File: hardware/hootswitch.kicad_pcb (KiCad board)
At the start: 2 copper layers, 100 x 88 mm, 127 parts, among them J1 Mini-DIN-4-G, J10 POWSEL, J11 TWI, J12 TWI, J2 Mini-DIN-4-G, J3 Mini-DIN-4-G, J4 Mini-DIN-4-G, J5 Mini-DIN-4-G, J6 Mini-DIN-4-G, J7 Barrel_Jack_MountingPin, J8 EXT_POW, J9 SW1, Q1 MMBT3904, Q10 MMBT3904, Q11 MMBT3904, Q12 MMBT3904, Q13 MMBT3904, Q14 MMBT3904, Q15 MMBT3904, Q16 MMBT3904, Q2 MMBT3904, Q3 MMBT3904, Q4 MMBT3904, Q5 MMBT3904, Q6 MMBT3904, Q7 MMBT3904, Q8 MMBT3904, Q9 MMBT3904, SW1 Switch1, U1 Pico, U10 LTV-357T, U11 LTV-357T, U2 LM1117-5.0, U3 ADuM1201AR, U4 ADuM1201AR, U5 ADuM1201AR, U6 ADuM1201AR, U7 ADuM1201AR, U8 LTV-357T, U9 LTV-357T

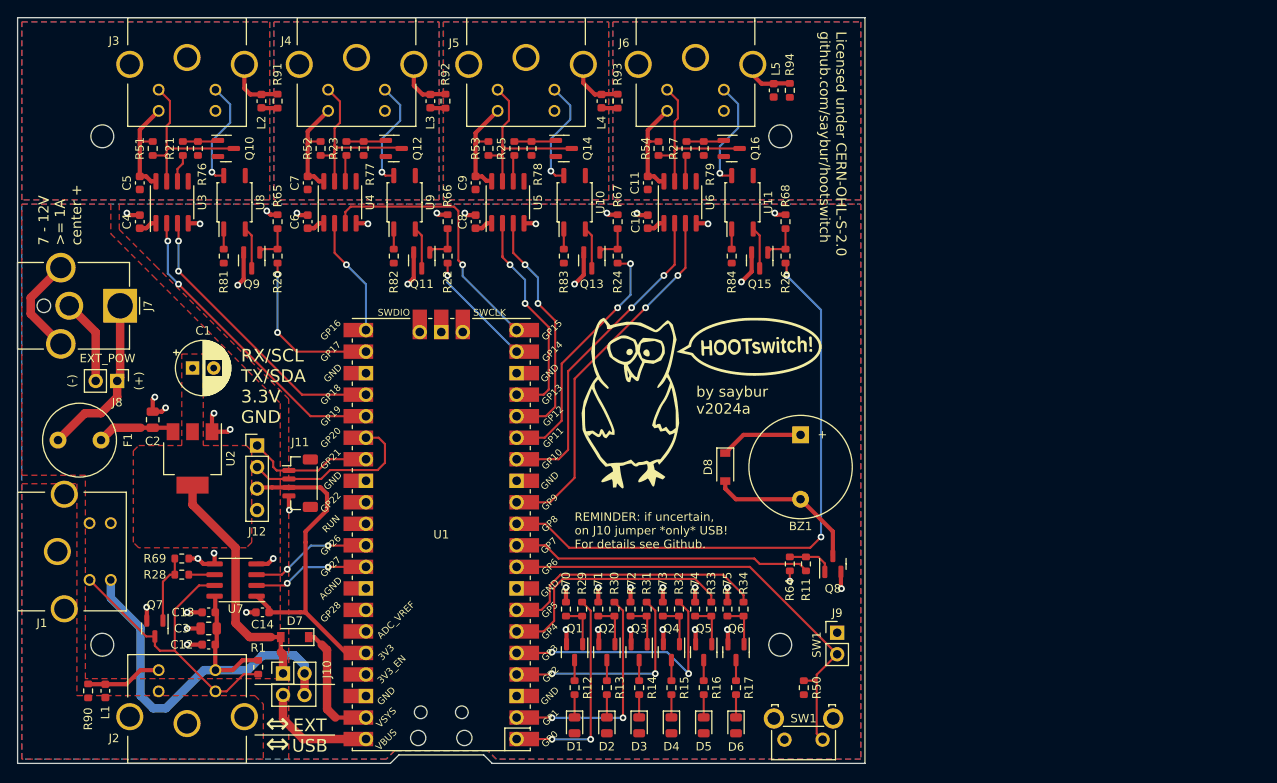
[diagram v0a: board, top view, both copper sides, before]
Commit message: Hardware Fork: Use Mosfets For Isolation
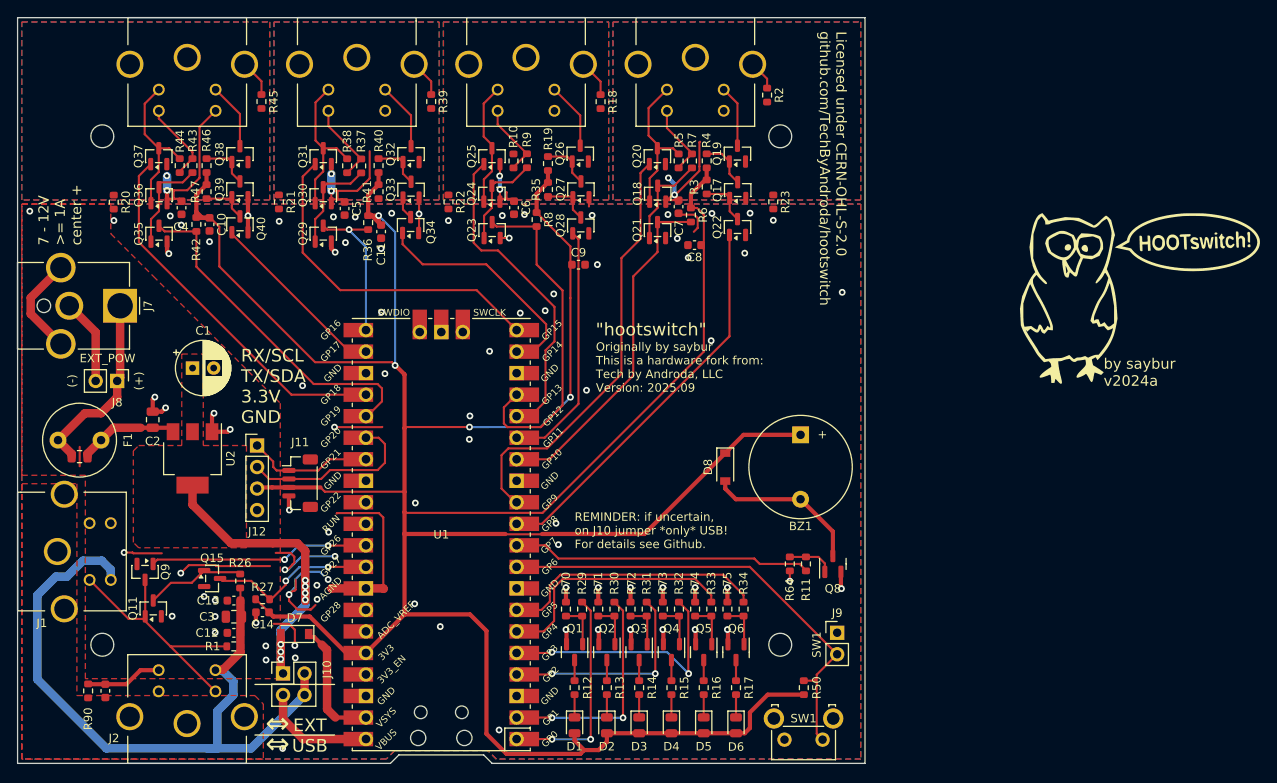
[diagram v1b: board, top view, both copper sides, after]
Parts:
- removed J3, J4, J5, J6: Mini-DIN-4-G, hootswitch:5749181-1
- removed L2, L3, L4, L5: DNP, Inductor_SMD:L_0603_1608Metric
- removed Q10, Q12, Q13, Q14, Q16, Q7: MMBT3904, Package_TO_SOT_SMD:SOT-23
- removed R24, R25, R28: 2K2, Resistor_SMD:R_0603_1608Metric
- removed R51, R52, R53, R54: 4K7, Resistor_SMD:R_0603_1608Metric
- removed R65, R66, R67, R68, R69, R76, R77, R78, R79: 10K, Resistor_SMD:R_0603_1608Metric
- removed R81, R82, R83, R84: 330, Resistor_SMD:R_0603_1608Metric
- removed R91, R92, R93, R94: 0, Resistor_SMD:R_0603_1608Metric
- removed U10, U11, U8, U9: LTV-357T, Package_SO:SO-4_4.4x3.9mm_P2.54mm
- removed U3, U4, U5, U6, U7: ADuM1201AR, Package_SO:SOIC-8_3.9x4.9mm_P1.27mm
- added F2: 500mA, Fuse:Fuse_0805_2012Metric, F.Cu at (67.3, 111.8)
- added J13: Mini-DIN-4-G, hootswitch:5749181-1, F.Cu at (140.0, 60.0)
- added J14: Mini-DIN-4-G, hootswitch:5749181-1, F.Cu at (120.0, 60.0)
- added J15: Mini-DIN-4-G, hootswitch:5749181-1, F.Cu at (100.0, 60.0)
- added J16: Mini-DIN-4-G, hootswitch:5749181-1, F.Cu at (80.0, 60.0)
- added Q17: 2N7002, Package_TO_SOT_SMD:SOT-23, F.Cu at (145.0, 80.3)
- added Q18: 2N7002, Package_TO_SOT_SMD:SOT-23, F.Cu at (135.5, 80.8)
- added Q19: 2N7002, Package_TO_SOT_SMD:SOT-23, F.Cu at (144.9, 76.0)
- added Q20: 2N7002, Package_TO_SOT_SMD:SOT-23, F.Cu at (135.5, 76.3)
- added Q21: 2N7002, Package_TO_SOT_SMD:SOT-23, F.Cu at (135.5, 85.1)
- added Q22: 2N7002, Package_TO_SOT_SMD:SOT-23, F.Cu at (145.0, 84.7)
- added Q23: 2N7002, Package_TO_SOT_SMD:SOT-23, F.Cu at (116.0, 85.1)
- added Q24: 2N7002, Package_TO_SOT_SMD:SOT-23, F.Cu at (116.0, 80.8)
- added Q25: 2N7002, Package_TO_SOT_SMD:SOT-23, F.Cu at (116.0, 76.3)
- added Q26: 2N7002, Package_TO_SOT_SMD:SOT-23, F.Cu at (126.4, 76.0)
- added Q27: 2N7002, Package_TO_SOT_SMD:SOT-23, F.Cu at (126.5, 80.3)
- added Q28: 2N7002, Package_TO_SOT_SMD:SOT-23, F.Cu at (126.5, 84.5)
- added Q29: 2N7002, Package_TO_SOT_SMD:SOT-23, F.Cu at (96.1, 85.5)
- added Q30: 2N7002, Package_TO_SOT_SMD:SOT-23, F.Cu at (96.1, 81.0)
- added Q31: 2N7002, Package_TO_SOT_SMD:SOT-23, F.Cu at (96.1, 76.3)
- added Q32: 2N7002, Package_TO_SOT_SMD:SOT-23, F.Cu at (106.4, 76.1)
- added Q33: 2N7002, Package_TO_SOT_SMD:SOT-23, F.Cu at (106.4, 80.3)
- added Q34: 2N7002, Package_TO_SOT_SMD:SOT-23, F.Cu at (106.4, 84.5)
- added Q35: 2N7002, Package_TO_SOT_SMD:SOT-23, F.Cu at (76.7, 85.5)
- added Q36: 2N7002, Package_TO_SOT_SMD:SOT-23, F.Cu at (76.7, 81.0)
- added Q37: 2N7002, Package_TO_SOT_SMD:SOT-23, F.Cu at (76.7, 76.3)
- added Q38: 2N7002, Package_TO_SOT_SMD:SOT-23, F.Cu at (86.2, 76.1)
- added Q39: 2N7002, Package_TO_SOT_SMD:SOT-23, F.Cu at (86.2, 80.3)
- added Q40: 2N7002, Package_TO_SOT_SMD:SOT-23, F.Cu at (86.2, 84.4)
- added R10: 4.7k, Resistor_SMD:R_0603_1608Metric, F.Cu at (118.5, 76.9)
- added R18: 33, Resistor_SMD:R_0603_1608Metric, F.Cu at (128.8, 69.9)
- added R19: 10k, Resistor_SMD:R_0603_1608Metric, F.Cu at (122.6, 77.2)
- added R2: 33, Resistor_SMD:R_0603_1608Metric, F.Cu at (148.4, 69.1)
- added R3: 10k, Resistor_SMD:R_0603_1608Metric, F.Cu at (141.3, 80.0)
- added R35: 10k, Resistor_SMD:R_0603_1608Metric, F.Cu at (122.6, 80.3)
- added R36: 1k, Resistor_SMD:R_0603_1608Metric, F.Cu at (101.4, 84.2)
- added R37: 4.7k, Resistor_SMD:R_0603_1608Metric, F.Cu at (100.5, 77.5)
- added R38: 4.7k, Resistor_SMD:R_0603_1608Metric, F.Cu at (98.9, 77.5)
- added R39: 33, Resistor_SMD:R_0603_1608Metric, F.Cu at (108.8, 69.9)
- added R4: 10k, Resistor_SMD:R_0603_1608Metric, F.Cu at (141.3, 76.9)
- added R40: 10k, Resistor_SMD:R_0603_1608Metric, F.Cu at (102.6, 77.5)
- added R41: 10k, Resistor_SMD:R_0603_1608Metric, F.Cu at (102.6, 80.5)
- added R42: 1k, Resistor_SMD:R_0603_1608Metric, F.Cu at (81.1, 84.4)
- added R43: 4.7k, Resistor_SMD:R_0603_1608Metric, F.Cu at (80.6, 77.5)
- added R44: 4.7k, Resistor_SMD:R_0603_1608Metric, F.Cu at (79.1, 77.5)
- added R45: 33, Resistor_SMD:R_0603_1608Metric, F.Cu at (88.8, 69.9)
- added R46: 10k, Resistor_SMD:R_0603_1608Metric, F.Cu at (82.3, 77.5)
- added R47: 10k, Resistor_SMD:R_0603_1608Metric, F.Cu at (82.3, 80.5)
- added R5: 4.7k, Resistor_SMD:R_0603_1608Metric, F.Cu at (138.0, 76.9)
- added R6: 1k, Resistor_SMD:R_0603_1608Metric, F.Cu at (139.5, 83.3)
- added R7: 4.7k, Resistor_SMD:R_0603_1608Metric, F.Cu at (139.6, 76.9)
- added R8: 1k, Resistor_SMD:R_0603_1608Metric, F.Cu at (121.2, 83.8)
- added R9: 4.7k, Resistor_SMD:R_0603_1608Metric, F.Cu at (120.1, 76.9)
- C10, C11, C8, C9: value 100nF -> 100N
- C4, C5, C6, C7: value 100nF -> 10n
- D7: value B5819W -> type="D" model="B5819W" lib=""
- Q11, Q15, Q9: value MMBT3904 -> 2N7002
- R20, R21, R22, R23, R26: value 2K2 -> 10k
- R27: value 2K2 -> 1k
- R90: value 0 -> 33
- moved R26 74.9 mm to (86.3, 126.5)
- moved Q15 74.7 mm to (83.0, 126.2), turned to 0 degrees
- moved R27 73.0 mm to (88.9, 128.6), turned to 0 degrees
- moved G*** 53.2 mm to (192.1, 93.1)
- moved Q11 51.9 mm to (76.0, 129.7), turned to 90 degrees
- moved C10 51.7 mm to (82.7, 84.4), turned to -90 degrees
- moved R23 50.8 mm to (149.2, 81.7), turned to -90 degrees
- moved C7 43.9 mm to (138.0, 82.3)
- moved Q9 38.9 mm to (75.0, 125.4)
- moved C11 32.0 mm to (102.9, 85.2)
- moved C8 26.0 mm to (139.9, 86.8), turned to 180 degrees
- moved C6 24.4 mm to (118.6, 82.4), turned to -90 degrees
- moved C5 24.4 mm to (98.6, 82.5)
- moved R20 20.4 mm to (71.3, 81.8), turned to -90 degrees
- moved C9 15.5 mm to (126.2, 89.2), turned to 0 degrees
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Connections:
- C11 pad 1: Net-(C11-Pad1) -> +3.3V
- C11 pad 2: Net-(C11-Pad2) -> GND
- C4 pad 1: +3.3V -> ADB1_GND
- C5 pad 1: Net-(C5-Pad1) -> ADB2_GND
- C5 pad 2: Net-(C5-Pad2) -> GND
- C6 pad 1: +3.3V -> ADB3_GND
- C7 pad 1: Net-(C7-Pad1) -> ADB4_GND
- C7 pad 2: Net-(C7-Pad2) -> GND
- C9 pad 1: Net-(C9-Pad1) -> +3.3V
- C9 pad 2: Net-(C9-Pad2) -> GND
- J1 pad 1: Net-(J2-Pad1) -> ADB_HOST_DAT
- J2 pad 1: Net-(J2-Pad1) -> ADB_HOST_DAT
- Q11 pad 1: Net-(Q11-Pad1) -> ADB_HOST_DAT
- Q11 pad 3: Net-(Q11-Pad3) -> Net-(Q11-D)
- Q15 pad 1: Net-(Q15-Pad1) -> Net-(Q11-D)
- Q15 pad 3: Net-(Q15-Pad3) -> /A_DI
- Q9 pad 1: Net-(Q9-Pad1) -> /A_DO
- Q9 pad 3: Net-(Q9-Pad3) -> ADB_HOST_DAT
- R1 pad 2: Net-(J2-Pad1) -> ADB_HOST_DAT
- R20 pad 1: /C1_PSW -> ADB1_GND
- R20 pad 2: Net-(Q9-Pad1) -> GND
- R21 pad 1: Net-(R21-Pad1) -> ADB2_GND
- R21 pad 2: Net-(Q10-Pad1) -> GND
- R22 pad 1: /C2_PSW -> ADB3_GND
- R22 pad 2: Net-(Q11-Pad1) -> GND
- R23 pad 1: Net-(R23-Pad1) -> ADB4_GND
- R23 pad 2: Net-(Q12-Pad1) -> GND
- R26 pad 1: /C4_PSW -> +5V
- R26 pad 2: Net-(Q15-Pad1) -> Net-(Q11-D)
- R27 pad 1: Net-(R27-Pad1) -> +3.3V
- R27 pad 2: Net-(Q16-Pad1) -> /A_DI
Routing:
- net +3.3V: track 58.0 -> 377.8 mm, vias 0 -> 4
- net GND: track 90.8 -> 138.2 mm, vias 43 -> 86
- net Net-(J2-Pad1): track 37.5 -> 0.00 mm
- net ADB_HOST_DAT: track 0.00 -> 31.3 mm
- net +5V: track 56.1 -> 86.0 mm
- net /C4_PSW: track 71.7 -> 46.2 mm, vias 2 -> 0
- net Net-(J4-Pad1): track 22.8 -> 0.00 mm
- net Net-(J5-Pad1): track 22.4 -> 0.00 mm
- net Net-(J3-Pad1): track 21.9 -> 0.00 mm
- net Net-(J6-Pad1): track 21.9 -> 0.00 mm
- net ADB1_GND: track 0.00 -> 19.2 mm, vias 0 -> 2
- net Net-(Q36-G): track 0.00 -> 18.1 mm
- net Net-(Q30-G): track 0.00 -> 18.1 mm
- net Net-(Q18-G): track 0.00 -> 17.7 mm
- net ADB2_GND: track 0.00 -> 15.6 mm, vias 0 -> 2
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- added copper zone on F.Cu, net ADB1_GND
- added copper zone on F.Cu, net ADB2_GND
- added copper zone on F.Cu, net ADB3_GND
- added copper zone on F.Cu, net ADB4_GND
- added copper zone on B.Cu, net Net-(J13-Pad5)
- added copper zone on B.Cu, net Net-(J14-Pad5)
- added copper zone on B.Cu, net Net-(J15-Pad5)
- added copper zone on B.Cu, net Net-(J16-Pad5)
- removed copper zone on F.Cu, net +3.3V
- removed copper zone on F.Cu, net Net-(C11-Pad2)
- removed copper zone on F.Cu, net Net-(C5-Pad2)
- removed copper zone on F.Cu, net Net-(C7-Pad2)
- removed copper zone on F.Cu, net Net-(C9-Pad2)
- removed copper zone on B.Cu, net Net-(J3-Pad5)
- removed copper zone on B.Cu, net Net-(J4-Pad5)
- removed copper zone on B.Cu, net Net-(J5-Pad5)
- removed copper zone on B.Cu, net Net-(J6-Pad5)
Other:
- board text added: "Licensed under CERN-OHL-S-2.0 github.com/TechByAndroda/hootswitch"
- board text added: "Originally by saybur This is a hardware fork from: Tech by Androda, LLC Version: 2025.09"
- board text added: "{dblquote}hootswitch{dblquote}"
- board text removed: "Licensed under CERN-OHL-S-2.0 github.com/saybur/hootswitch"
